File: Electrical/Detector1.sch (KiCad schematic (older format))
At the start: 36 parts

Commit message: Small changes...
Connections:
- net HS: now reaches D?.3
- net Det: now reaches R?.2
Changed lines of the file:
@@
-EESchema Schematic File Version 2  date 4/15/2013 9:49:50 PM
+EESchema Schematic File Version 2  date 4/17/2013 7:49:12 PM
 LIBS:power
 LIBS:device
@@
 $Descr A4 11700 8267
 encoding utf-8
-Sheet 4 5
+Sheet 4 6
 Title "Cosmic Ray Detector"
-Date "16 apr 2013"
+Date "17 apr 2013"
 Rev "1A"
 Comp "Ethan Harstad"
@@
 Comment4 ""
 $EndDescr
+Text HLabel 10700 900  2    60   Output ~ 0
+HS
+Text HLabel 10700 2300 2    60   Output ~ 0
+Det
 Connection ~ 4900 3300
 Wire Wire Line

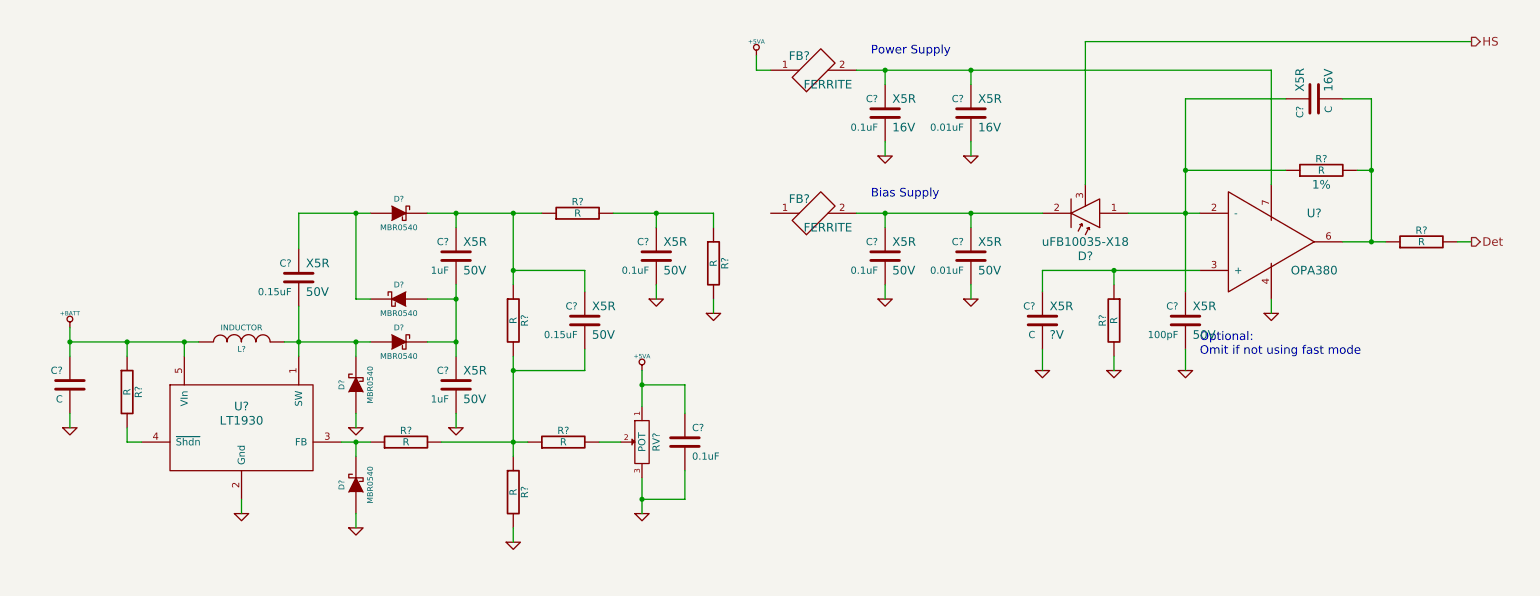
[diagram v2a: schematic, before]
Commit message: Added voltage references and test points
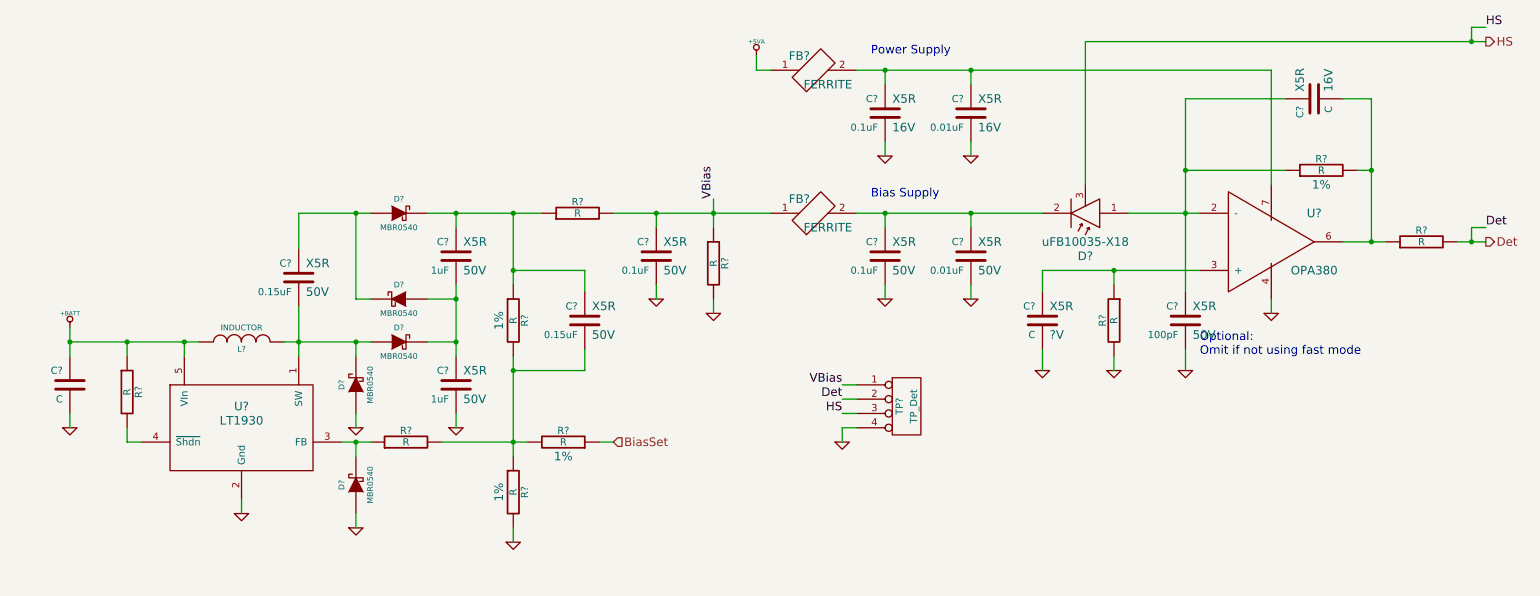
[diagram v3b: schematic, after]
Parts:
- removed C?: 0.1uF, symbol C
- removed R? (x2): R, symbol R
- removed RV?: POT, symbol POT
- added R? (x2): R, symbol R
- added TP?: TP_Det, symbol CONN_4
- R?: Tolerance (none) -> 1%
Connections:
- net Det: now also TP?.2 (P2)
- net GND: now also R?.2, TP?.4 (P4)
- net HS: now also TP?.3 (P3)
- net VBias: now reaches FB?.1
- net VBias: now also C?.1, R?.1, R?.2, TP?.1 (P1)
- net at C?.2, R?.2, R?.2: now also R?.1, R?.2
- new net BiasSet: R?.1

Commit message: Adding schematic annotations to explain functions
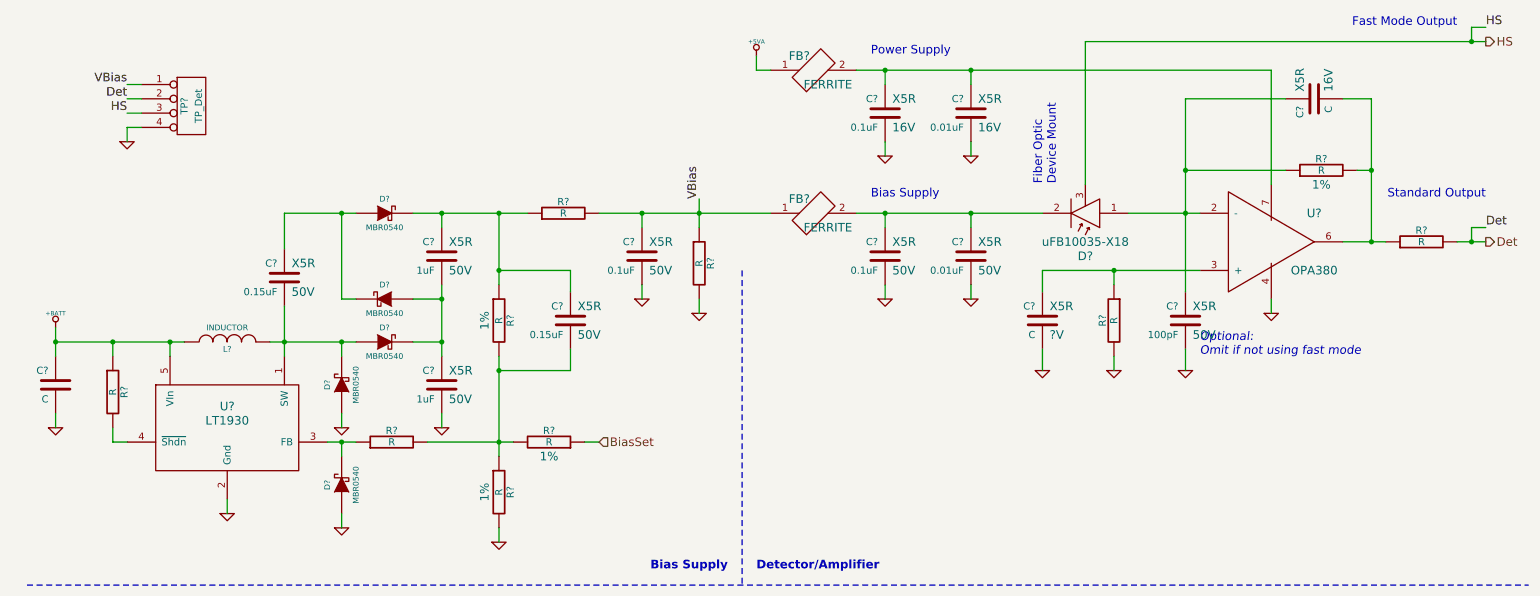
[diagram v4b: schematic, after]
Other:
- note added: "Detector/Amplifier"
- note added: "Fast Mode Output"
- note added: "Fiber Optic\nDevice Mount"
- note added: "Standard Output"
- moved on the sheet: C?, D?, L?, R?, TP?, U?

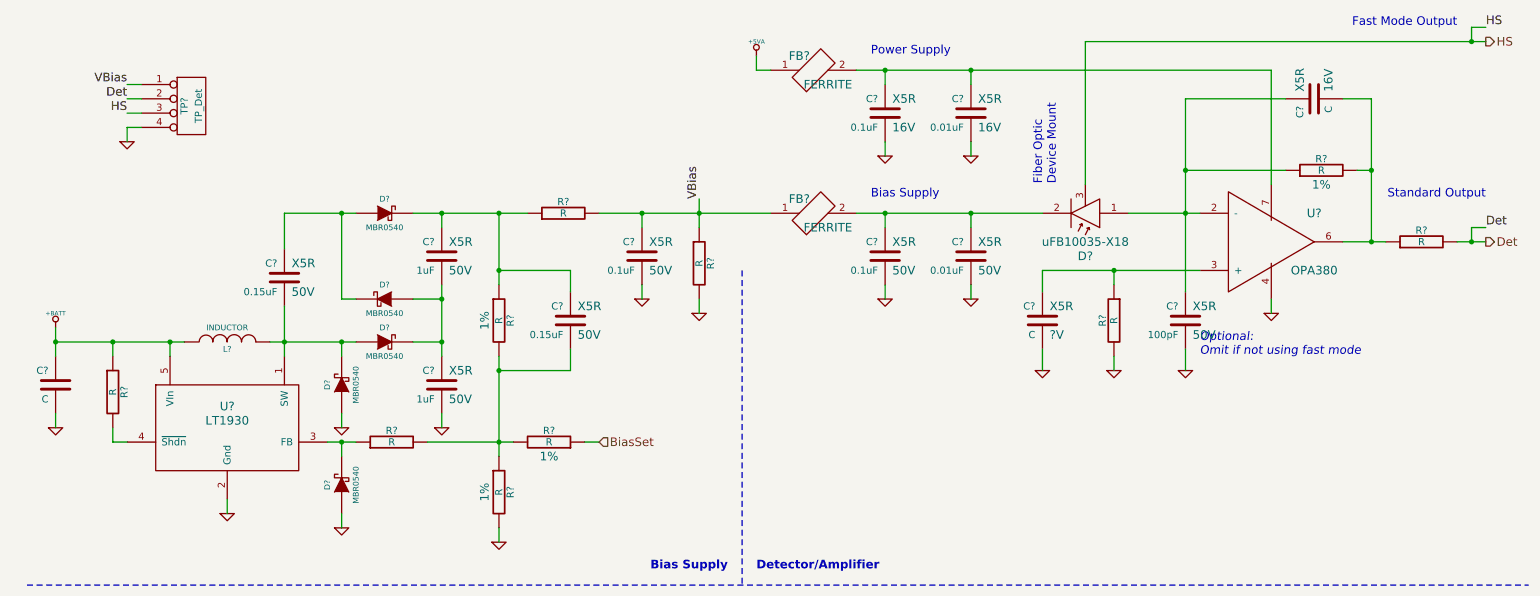
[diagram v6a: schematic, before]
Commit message: Added sensors/data logger with ChipKit Max
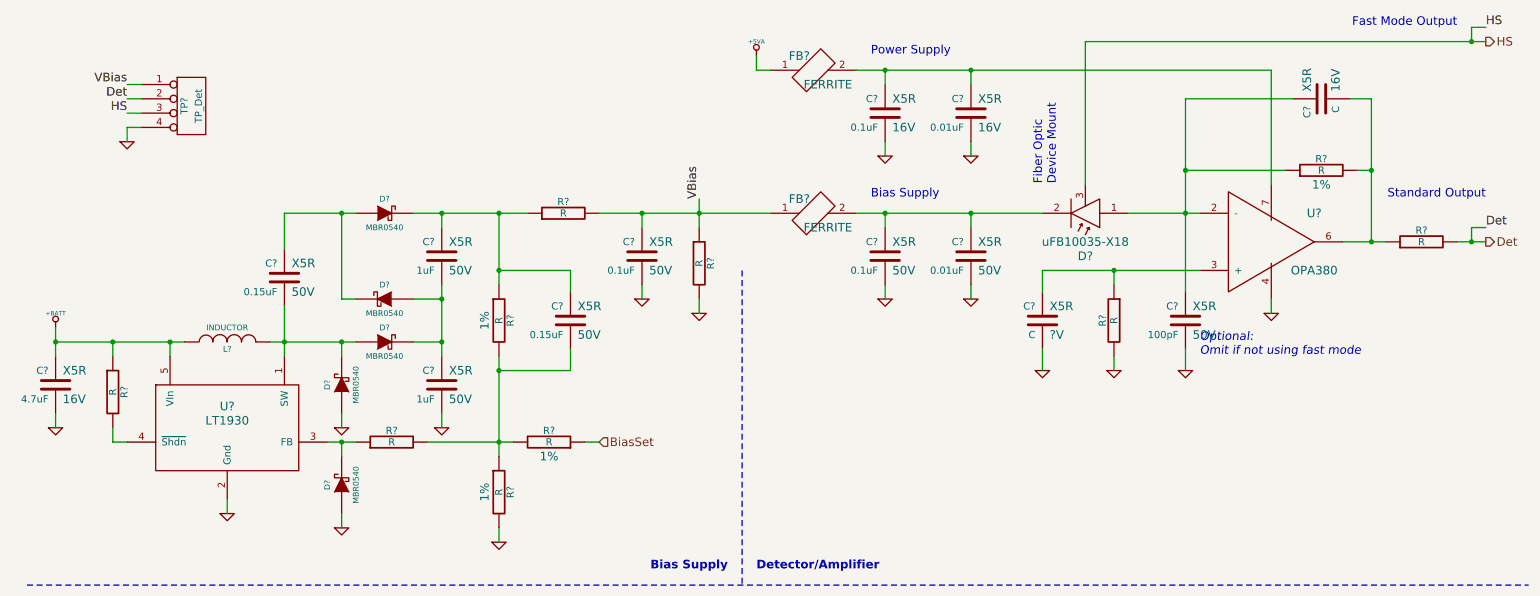
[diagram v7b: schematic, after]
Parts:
- C?: value C -> 4.7uF; Dielectric (none) -> X5R; Voltage (none) -> 16V
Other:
- moved on the sheet: C?
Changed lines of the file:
@@
-EESchema Schematic File Version 2  date 4/19/2013 7:14:36 PM
+EESchema Schematic File Version 2  date 5/4/2013 6:32:29 PM
 LIBS:power
 LIBS:device
@@
 $Descr A4 11700 8267
 encoding utf-8
-Sheet 5 6
+Sheet 3 7
 Title "Cosmic Ray Detector"
-Date "20 apr 2013"
+Date "4 may 2013"
 Rev "1A"
 Comp "Ethan Harstad"
@@
 Connection ~ 5300 2100
 Wire Wire Line
-	5300 2000 5300 2200
+	5300 2000 5300 2100
+Wire Wire Line
+	5300 2100 5300 2200
 Wire Wire Line
 	4500 3700 4600 3700
@@
 Connection ~ 3900 2100
 Wire Wire Line
-	4100 2100 3300 2100
+	4100 2100 3900 2100
+Wire Wire Line
+	3900 2100 3500 2100
+Wire Wire Line
+	3500 2100 3300 2100
 Connection ~ 3900 2500
 Wire Wire Line
@@
 Connection ~ 3900 3700
 Wire Wire Line
-	3900 3100 3900 3800
+	3900 3100 3900 3200
+Wire Wire Line
+	3900 3200 3900 3700
+Wire Wire Line
+	3900 3700 3900 3800
 Wire Wire Line
 	3500 3600 3500 3500
@@
 	2800 2700 2900 2700
 Wire Wire Line
-	2400 2750 2400 3100
-Wire Wire Line
-	3500 2600 3500 3100
-Wire Wire Line
-	2900 2100 2400 2100
+	2400 2750 2400 3000
+Wire Wire Line
+	2400 3000 2400 3100
+Wire Wire Line
+	3500 2600 3500 2700
+Wire Wire Line
+	3500 2700 3500 3000
+Wire Wire Line
+	3500 3000 3500 3100
+Wire Wire Line
+	2900 2100 2800 2100
+Wire Wire Line
+	2800 2100 2400 2100
 Wire Wire Line
 	2400 2100 2400 2350
@@
 Connection ~ 800  3000
 Wire Wire Line
-	1700 3000 800  3000
-Wire Wire Line
-	10800 2300 10600 2300
-Wire Wire Line
-	6400 1100 9300 1100
-Wire Wire Line
-	8300 2100 8800 2100
-Wire Wire Line
-	8700 2650 8700 1300
+	1700 3000 1600 3000
+Wire Wire Line
+	1600 3000 1200 3000
+Wire Wire Line
+	1200 3000 800  3000
+Wire Wire Line
+	10800 2300 10700 2300
+Wire Wire Line
+	10700 2300 10600 2300
+Wire Wire Line
+	6400 1100 6600 1100
+Wire Wire Line
+	6600 1100 7200 1100
+Wire Wire Line
+	7200 1100 9300 1100
+Wire Wire Line
+	8300 2100 8700 2100
+Wire Wire Line
+	8700 2100 8800 2100
+Wire Wire Line
+	8700 2650 8700 2100
+Wire Wire Line
+	8700 2100 8700 1800
+Wire Wire Line
+	8700 1800 8700 1300
 Wire Wire Line
 	8200 3100 8200 3200
@@
 	6600 1100 6600 1200
 Wire Wire Line
-	7700 2100 6400 2100
+	7700 2100 7200 2100
+Wire Wire Line
+	7200 2100 6600 2100
+Wire Wire Line
+	6600 2100 6400 2100
 Connection ~ 10000 1800
 Wire Wire Line
-	10000 2300 10000 1300
-Wire Wire Line
-	10000 1300 9800 1300
+	10000 2300 10000 1800
+Wire Wire Line
+	10000 1800 10000 1300
+Wire Wire Line
+	10000 1300 9850 1300
 Connection ~ 8700 2100
 Wire Wire Line
@@
 	9900 1800 10000 1800
 Wire Wire Line
-	9800 2300 10100 2300
+	9800 2300 10000 2300
+Wire Wire Line
+	10000 2300 10100 2300
 Wire Wire Line
 	7700 2650 7700 2500
 Wire Wire Line
-	8700 1300 9400 1300
+	8700 1300 9450 1300
 Connection ~ 8700 1800
 Wire Wire Line
@@
 	8700 3200 8700 3050
 Wire Wire Line
-	7700 2500 8800 2500
+	7700 2500 8200 2500
+Wire Wire Line
+	8200 2500 8800 2500
 Wire Wire Line
 	8000 1900 8000 900
 Wire Wire Line
-	8000 900  10800 900
+	8000 900  10700 900
+Wire Wire Line
+	10700 900  10800 900
 Wire Wire Line
 	5700 1000 5700 1100
@@
 	5700 1100 5800 1100
 Wire Wire Line
-	800  3100 800  2900
+	800  3100 800  3000
+Wire Wire Line
+	800  3000 800  2900
 Wire Wire Line
 	1600 3100 1600 3000
@@
 	2000 4200 2000 4100
 Wire Wire Line
-	2900 3700 2700 3700
+	2900 3700 2800 3700
+Wire Wire Line
+	2800 3700 2700 3700
 Wire Wire Line
 	2800 3600 2800 3500
 Wire Wire Line
-	2900 3000 2300 3000
+	2900 3000 2800 3000
+Wire Wire Line
+	2800 3000 2400 3000
+Wire Wire Line
+	2400 3000 2300 3000
 Connection ~ 2400 3000
 Wire Wire Line
@@
 Connection ~ 3500 2700
 Wire Wire Line
-	3900 2600 3900 2100
+	3900 2600 3900 2500
+Wire Wire Line
+	3900 2500 3900 2100
 Connection ~ 3500 2100
 Wire Wire Line
 	3900 4400 3900 4300
 Wire Wire Line
-	3400 3700 4000 3700
+	3400 3700 3900 3700
+Wire Wire Line
+	3900 3700 4000 3700
 Wire Wire Line
 	4400 3050 4400 3200
@@
 	1300 1500 1300 1600
 Wire Wire Line
-	5800 2100 4600 2100
+	5800 2100 5300 2100
+Wire Wire Line
+	5300 2100 4900 2100
+Wire Wire Line
+	4900 2100 4600 2100
 Wire Wire Line
 	10800 2200 10700 2200
@@
 P 800 3300
 F 0 "C?" H 850 3400 50  0000 L CNN
-F 1 "C" H 850 3200 50  0000 L CNN
+F 1 "4.7uF" H 850 3200 50  0000 L CNN
+F 4 "16V" H 750 3200 60  0000 R CNN "Voltage"
+F 5 "X5R" H 750 3400 60  0000 R CNN "Dielectric"
 	1    800  3300
 	-1   0    0    -1
@@
 L C C?
 U 1 1 516B74F8
-P 9600 1300
-F 0 "C?" H 9650 1400 50  0000 L CNN
-F 1 "C" H 9650 1200 50  0000 L CNN
-F 4 "16V" H 9550 1200 60  0000 R CNN "Voltage"
-F 5 "X5R" H 9550 1400 60  0000 R CNN "Dielectric"
-	1    9600 1300
+P 9650 1300
+F 0 "C?" H 9700 1400 50  0000 L CNN
+F 1 "C" H 9700 1200 50  0000 L CNN
+F 4 "16V" H 9600 1200 60  0000 R CNN "Voltage"
+F 5 "X5R" H 9600 1400 60  0000 R CNN "Dielectric"
+	1    9650 1300
 	0    -1   1    0
 $EndComp

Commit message: Annotated schematic
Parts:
- gave numbers to parts that had none: 35
